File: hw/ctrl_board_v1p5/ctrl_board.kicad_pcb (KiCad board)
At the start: 2 copper layers, 65 x 33 mm, 33 parts, among them J1 RaSCSI Connector, J2 OLED Connector, J3 Conn_02x06_Odd_Even, P1 Conn_02x20_Odd_Even, SW1 SW_SPST, SW2 SW_SPST, SW4 Rotary_Encoder_Switch, U1 PCA9554APW,118

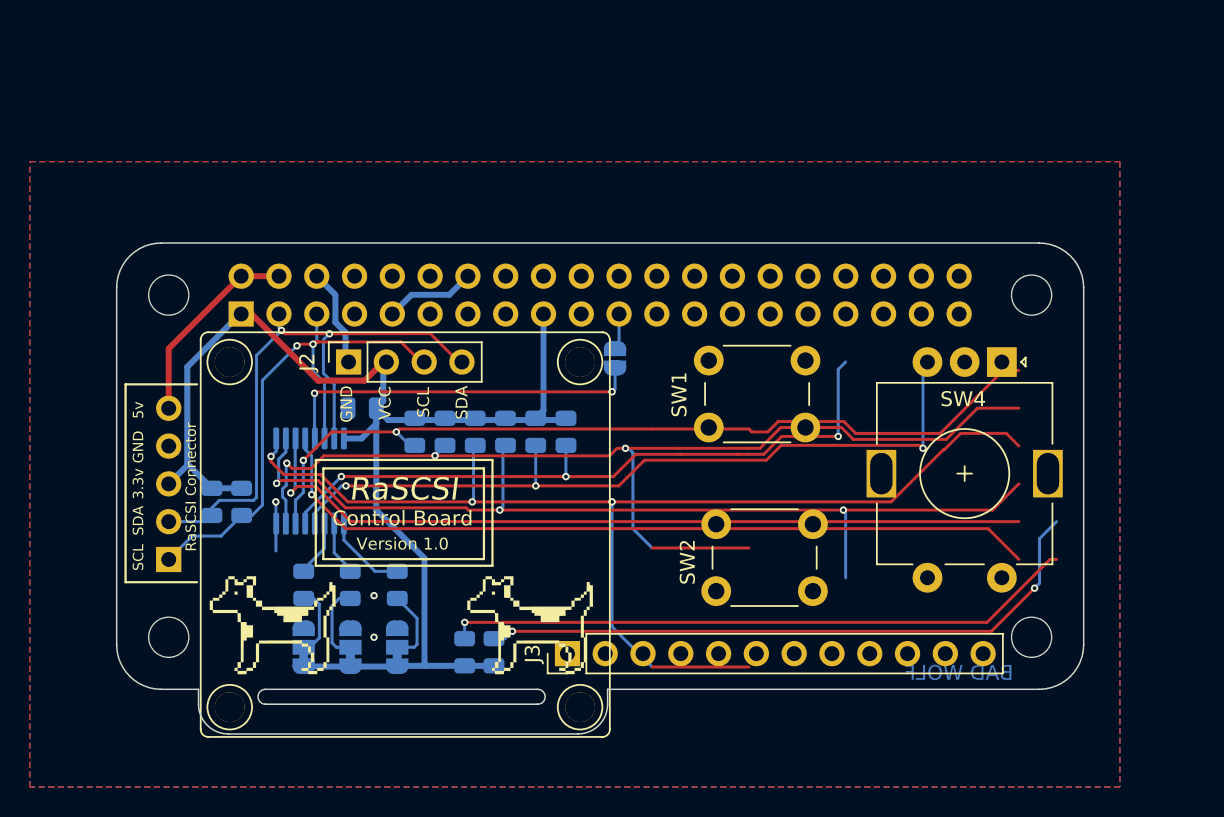
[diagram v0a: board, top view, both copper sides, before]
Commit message: Updated to Kicad 6.0
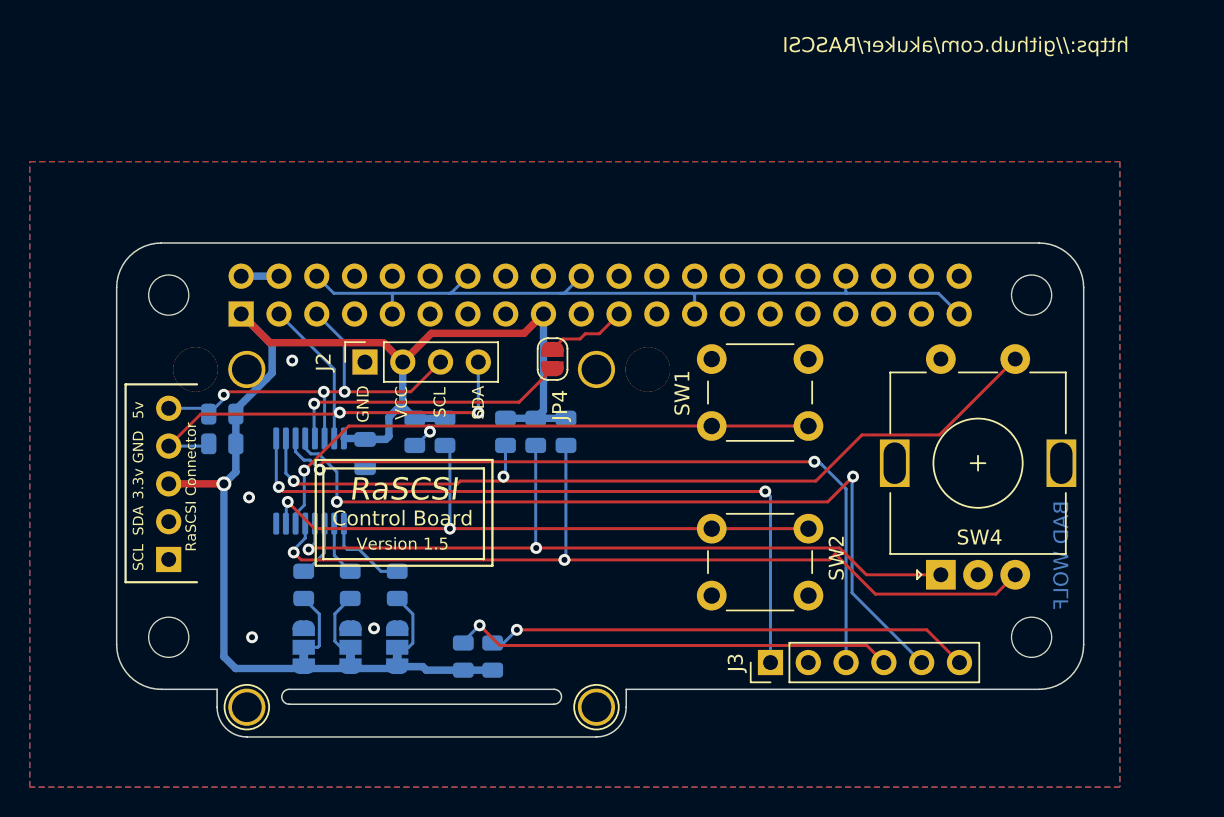
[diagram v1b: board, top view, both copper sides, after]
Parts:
- removed G*** (x2): LOGO, mousebites:dogcow
- removed G***: LOGO, mousebites:pi_logo
- removed R5: 10k, Resistor_SMD:R_0805_2012Metric
- J2: footprint mousebites:0.9_in_OLED_Footprint -> mousebites:0.9_and_1.3_in_OLED_Footprint
- J3: value Conn_02x06_Odd_Even -> Conn_01x06_Odd_Even; footprint Connector_PinHeader_2.54mm:PinHeader_1x12_P2.54mm_Vertical -> Connector_PinHeader_2.54mm:PinHeader_1x06_P2.54mm_Vertical
- JP4: moved to F.Cu
- moved SW4 14.9 mm to (255.4, 116.3), turned to 90 degrees
- moved J3 13.7 mm to (243.9, 122.2)
- moved SW2 7.84 mm to (246.5, 117.7), turned to 180 degrees
- moved R10 6.04 mm to (207.1, 105.5), turned to 0 degrees
- moved JP4 4.20 mm to (229.3, 101.8)
- moved R11 3.96 mm to (207.1, 107.5), turned to 180 degrees
- moved C1 3.06 mm to (216.7, 108.2), turned to -90 degrees
- moved R12 2.09 mm to (223.3, 121.8), turned to 90 degrees
- moved R13 1.91 mm to (225.3, 121.8), turned to 90 degrees
- moved J2 1.10 mm to (220.5, 102.0)
- moved SW1 0.22 mm to (240.0, 101.8)
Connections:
- J1 pad 1: Net-(J1-Pad1) -> unconnected-(J1-Pad1)
- J3 pad 1: /BUTTON_1 -> /BUTTON_3
- J3 pad 3: /BUTTON_2 -> /LED_1
- J3 pad 4: GND -> Net-(J3-Pad4)
- J3 pad 5: /BUTTON_3 -> /LED_2
- J3 pad 6: GND -> Net-(J3-Pad6)
- R12 pad 1: Net-(J3-Pad10) -> +3V3
- R12 pad 2: +3V3 -> Net-(J3-Pad4)
- R13 pad 1: Net-(J3-Pad12) -> +3V3
- R13 pad 2: +3V3 -> Net-(J3-Pad6)
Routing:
- net Net-(J3-Pad12): track 42.9 -> 0.00 mm, vias 1 -> 0
- net Net-(J3-Pad10): track 42.8 -> 0.00 mm, vias 2 -> 0
- net GND: track 16.0 -> 51.9 mm, vias 3 -> 4
- net Net-(J3-Pad6): track 0.00 -> 32.7 mm, vias 0 -> 1
- net /BUTTON_3: track 77.9 -> 47.8 mm, vias 3 -> 2
- net Net-(J3-Pad4): track 0.00 -> 29.8 mm, vias 0 -> 1
- net /BUTTON_2: track 71.0 -> 43.0 mm, vias 3 -> 2
- net /BUTTON_1: track 57.5 -> 40.8 mm
- net /ROTARY_ENC_B: track 46.0 -> 60.5 mm, vias 3 -> 2
- net +5V: track 13.4 -> 2.54 mm
- net /GPIO3(SCL1): track 38.2 -> 29.2 mm, vias 2 -> 3
- net /BUTTON_4: track 63.8 -> 57.7 mm, vias 3 -> 2
- net Net-(JP4-Pad1): track 24.8 -> 19.4 mm, vias 2 -> 1
- net +3V3: track 88.9 -> 93.6 mm, vias 0 -> 1
- net /GPIO9(SPI0_MISO): track 2.44 -> 5.46 mm
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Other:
- board size 65 x 33 mm -> 65 x 33.2 mm
- net class Default removed
- net class Power removed
- board text added: "Version 1.5"
- board text added: "https://github.com/akuker/RASCSI"
- board text removed: "BTN1"
- board text removed: "BTN2"
- board text removed: "BTN4"
- board text removed: "Version 1.0"
- board text removed: "https://github.com/akuker/RASCSI/"

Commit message: Genereated Gerber Files
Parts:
- added G***: LOGO, mousebites:pi_logo, F.Cu at (230.1, 111.9)
- added G***: LOGO, mousebites:pi_logo, F.Cu at (211.7, 112.1)
- added REF**: KiCad-Logo2_5mm_SilkScreen, Symbol:KiCad-Logo2_5mm_SilkScreen, F.Cu at (220.5, 120.0)
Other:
- board text added: "OLED I2C Connector"

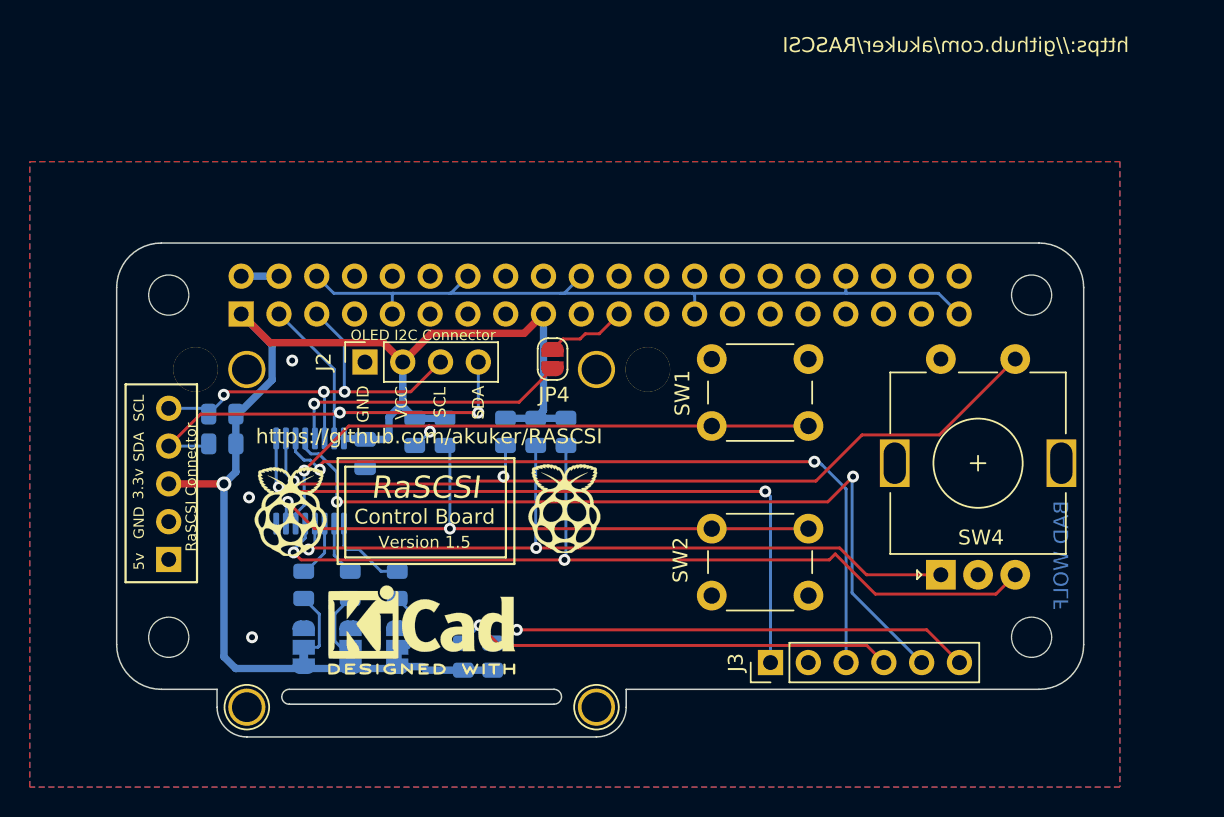
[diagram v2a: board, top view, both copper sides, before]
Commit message: Fixed order of RaSCSI connector pinout & cleanup
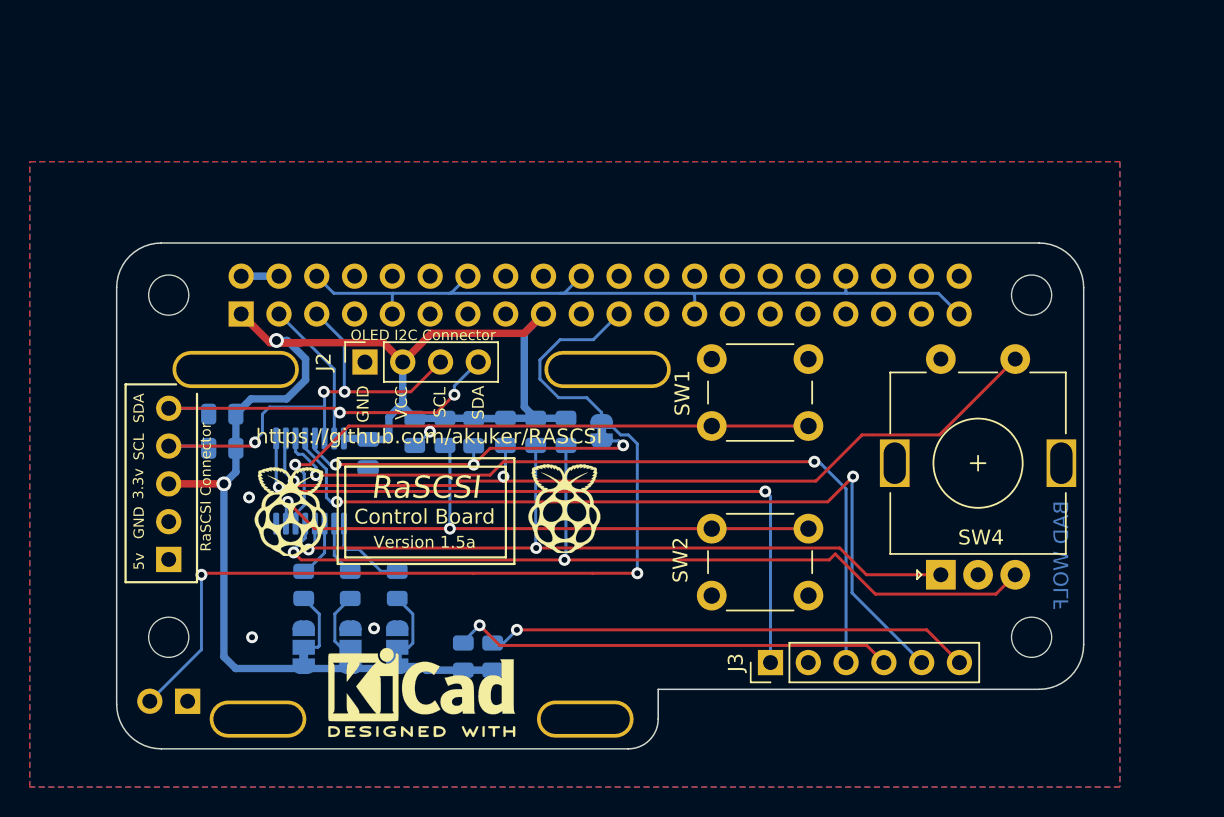
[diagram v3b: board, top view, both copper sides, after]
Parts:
- added G4: DogCow, mousebites:dogcow, B.Cu at (257.9, 111.2)
- added J4: Aux GPIO Connector, Connector_PinHeader_2.54mm:PinHeader_1x02_P2.54mm_Vertical, B.Cu at (204.8, 124.8)
- added R5: 10k, Resistor_SMD:R_0805_2012Metric, B.Cu at (224.0, 106.7)
- G1, G2: renamed from G***; value LOGO -> Pi Logo
- G3: renamed from REF**; value KiCad-Logo2_5mm_SilkScreen -> KiCad Logo
- JP4: footprint Jumper:SolderJumper-2_P1.3mm_Open_RoundedPad1.0x1.5mm -> Jumper:SolderJumper-2_P1.3mm_Bridged_RoundedPad1.0x1.5mm; moved to B.Cu
- MK1, MK2, MK4: moved to B.Cu
- moved JP4 5.87 mm to (232.6, 106.7)
- moved G3 4.20 mm to (220.5, 124.2)
- moved R10 2.30 mm to (207.1, 107.8)
- moved R11 2.00 mm to (207.1, 105.5)
- moved C1 0.20 mm to (216.9, 108.2)
- turned MK1 to 0 degrees
- turned MK2 to 0 degrees
- turned MK4 to 180 degrees
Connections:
- J1 pad 4: /GPIO2(SDA1) -> /GPIO3(SCL1)
- J1 pad 5: /GPIO3(SCL1) -> /GPIO2(SDA1)
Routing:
- net /GPIO9(SPI0_MISO): track 5.46 -> 64.6 mm, vias 0 -> 2
- net +3V3: track 94.0 -> 101.0 mm, vias 1 -> 2
- net Net-(JP4-Pad1): track 19.4 -> 25.3 mm, vias 1 -> 3
- net /GPIO3(SCL1): track 29.2 -> 33.0 mm
- net /GPIO2(SDA1): track 38.2 -> 35.9 mm
- net /BUTTON_1: track 40.8 -> 41.8 mm
- net GND: vias 4 -> 3
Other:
- board size 65 x 33.2 mm -> 65 x 34 mm
- board text added: "Note: Some mounting holes are {dblquote}flipped{dblquote} to prevent Courtyard overlap warnings"
- board text added: "Version 1.5a"
- board text removed: "Version 1.5"
